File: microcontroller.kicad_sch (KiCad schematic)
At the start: 2 parts, among them U4 ESP32-S3-WROOM-1, Y1 Crystal_GND24

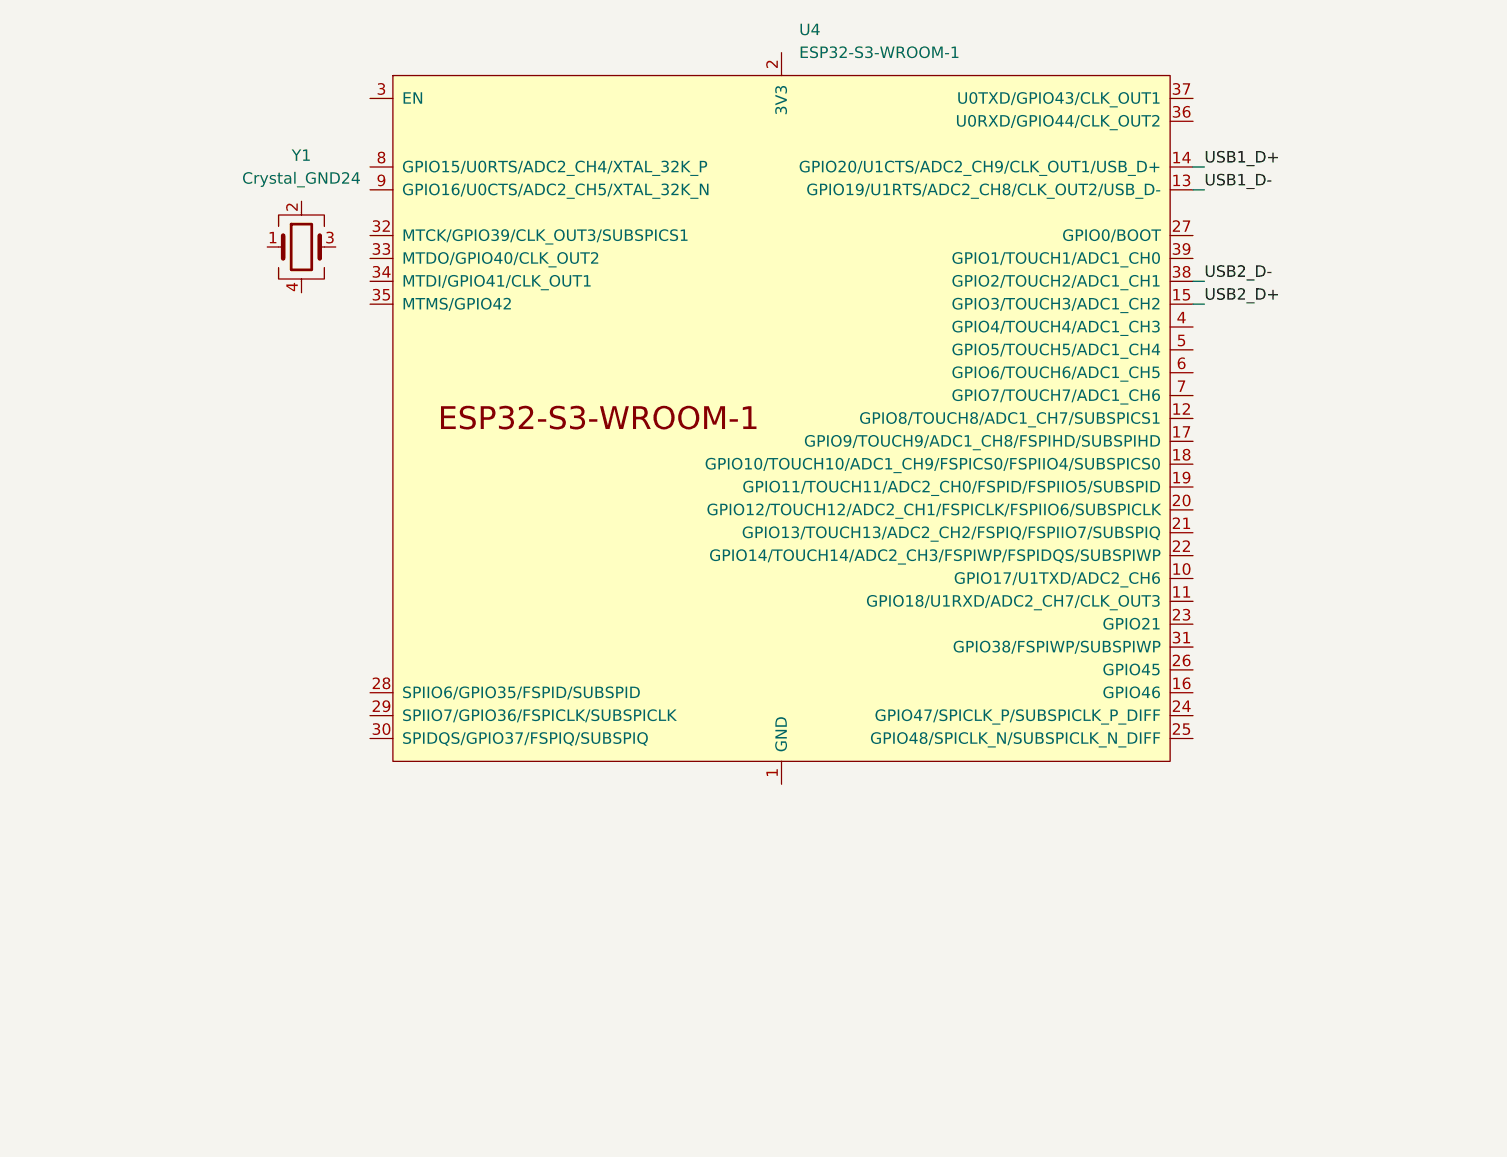
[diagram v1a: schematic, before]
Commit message: reworked component naming
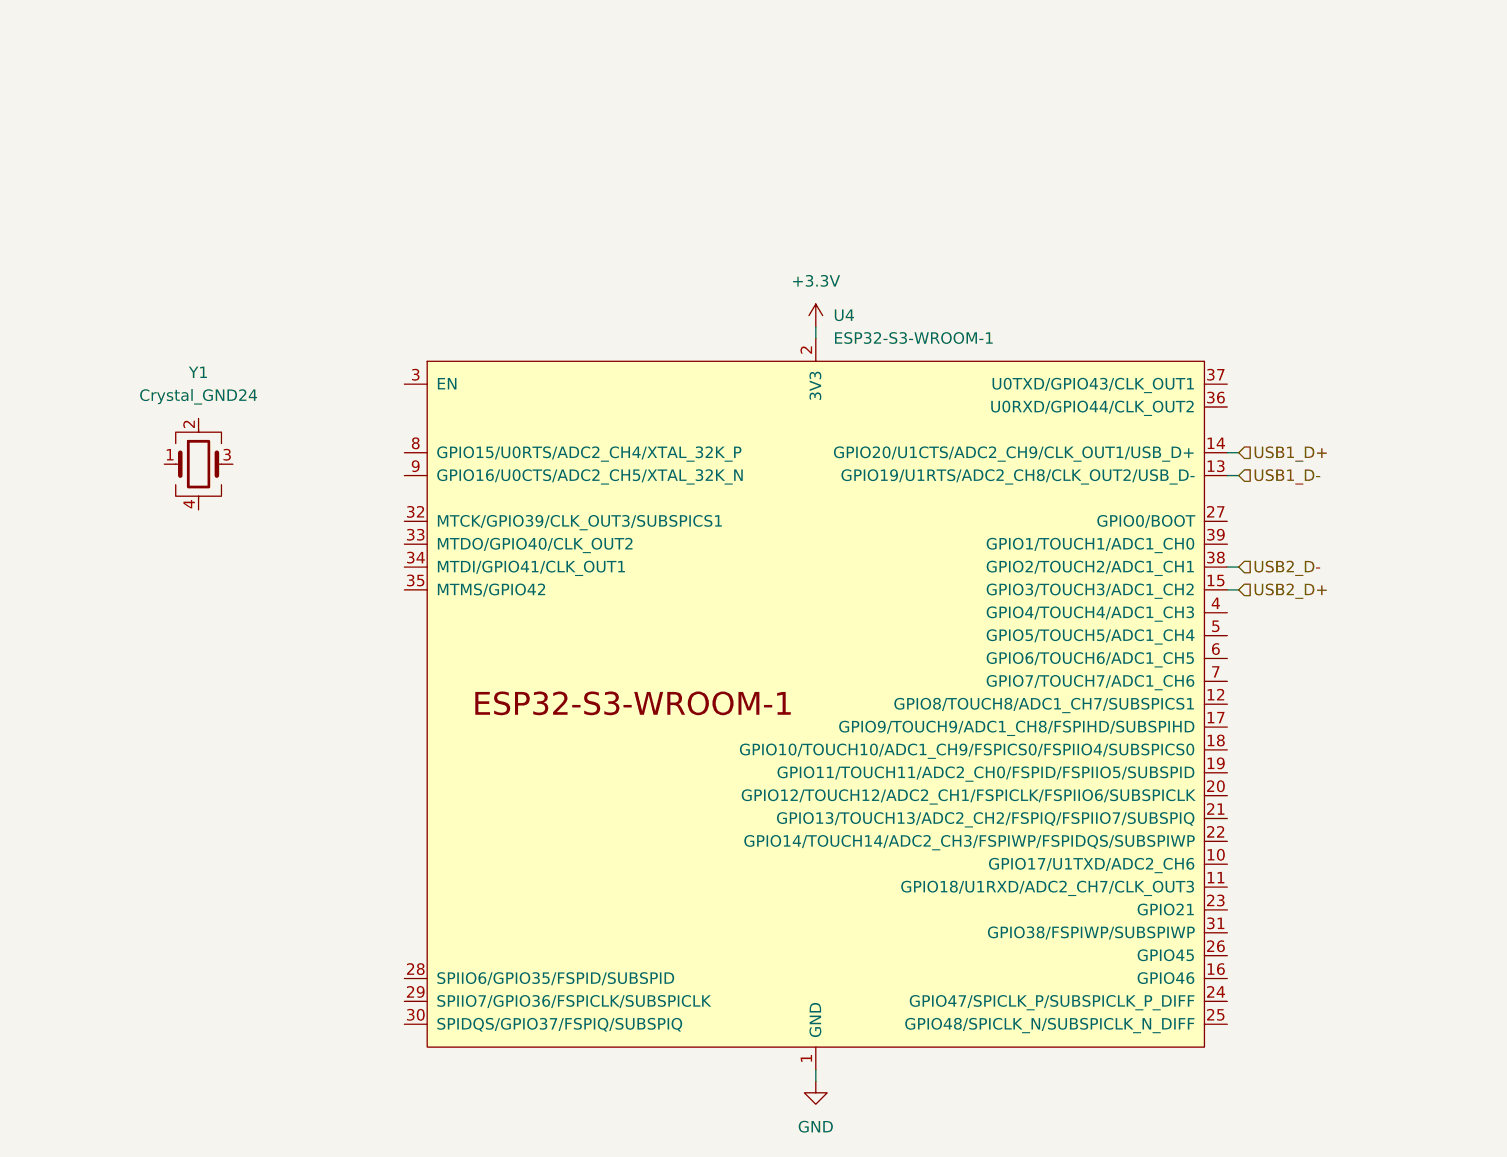
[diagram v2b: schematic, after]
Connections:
- net GND: now reaches U4.1 (GND), U4.40 (GND), U4.41 (GND)
- net +3.3V: now reaches U4.2 (3V3)
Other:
- moved on the sheet: U4, Y1
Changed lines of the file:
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@@
 (kicad_sch (version 20230121) (generator eeschema)
   (paper "A4")
-  (wire (pts (xy 156.21 50.8) (xy 154.94 50.8))
+  (wire (pts (xy 113.03 152.4) (xy 113.03 151.13))
     (stroke (width 0) (type default))
   )
-  (wire (pts (xy 156.21 63.5) (xy 154.94 63.5))
+  (wire (pts (xy 160.02 97.79) (xy 158.75 97.79))
     (stroke (width 0) (type default))
   )
-  (wire (pts (xy 154.94 53.34) (xy 156.21 53.34))
+  (wire (pts (xy 160.02 85.09) (xy 158.75 85.09))
     (stroke (width 0) (type default))
   )
-  (wire (pts (xy 156.21 66.04) (xy 154.94 66.04))
+  (wire (pts (xy 113.03 68.58) (xy 113.03 69.85))
     (stroke (width 0) (type default))
   )
-  (label "USB1_D+" (at 156.21 50.8 0) (fields_autoplaced)
-    (effects (font (size 1.27 1.27)) (justify left bottom))
+  (wire (pts (xy 160.02 82.55) (xy 158.75 82.55))
+    (stroke (width 0) (type default))
   )
-  (label "USB1_D-" (at 156.21 53.34 0) (fields_autoplaced)
-    (effects (font (size 1.27 1.27)) (justify left bottom))
+  (wire (pts (xy 160.02 95.25) (xy 158.75 95.25))
+    (stroke (width 0) (type default))
   )
-  (label "USB2_D+" (at 156.21 66.04 0) (fields_autoplaced)
-    (effects (font (size 1.27 1.27)) (justify left bottom))
+  (hierarchical_label "USB1_D-" (shape input) (at 160.02 85.09 0) (fields_autoplaced)
+    (effects (font (size 1.27 1.27)) (justify left))
   )
-  (label "USB2_D-" (at 156.21 63.5 0) (fields_autoplaced)
-    (effects (font (size 1.27 1.27)) (justify left bottom))
+  (hierarchical_label "USB1_D+" (shape input) (at 160.02 82.55 0) (fields_autoplaced)
+    (effects (font (size 1.27 1.27)) (justify left))
   )
-  (symbol (lib_id "Device:Crystal_GND24") (at 55.88 59.69 0) (unit 1)
-    (in_bom yes) (on_board yes) (dnp no)
-    (property "Reference" "Y1" (at 55.88 49.53 0)
+  (hierarchical_label "USB2_D+" (shape input) (at 160.02 97.79 0) (fields_autoplaced)
+    (effects (font (size 1.27 1.27)) (justify left))
+  )
+  (hierarchical_label "USB2_D-" (shape input) (at 160.02 95.25 0) (fields_autoplaced)
+    (effects (font (size 1.27 1.27)) (justify left))
+  )
+  (symbol (lib_id "power:+3.3V") (at 113.03 68.58 0) (unit 1)
+    (in_bom yes) (on_board yes) (dnp no) (fields_autoplaced)
+    (property "Reference" "#PWR022" (at 113.03 72.39 0)
+      (effects (font (size 1.27 1.27)) hide)
+    )
+    (property "Value" "+3.3V" (at 113.03 63.5 0)
       (effects (font (size 1.27 1.27)))
     )
-    (property "Value" "Crystal_GND24" (at 55.88 52.07 0)
+    (property "Footprint" "" (at 113.03 68.58 0)
+      (effects (font (size 1.27 1.27)) hide)
+    )
+    (property "Datasheet" "" (at 113.03 68.58 0)
+      (effects (font (size 1.27 1.27)) hide)
+    )
+    (pin "1")
+    (instances
+      (project "Lily58"
+        (path "/a0958e12-2248-4ac3-b259-3086ac296b70"
+          (reference "#PWR022") (unit 1)
+        )
+        (path "/a0958e12-2248-4ac3-b259-3086ac296b70/e89ddc09-3400-44c0-8130-3ab15c16d278"
+          (reference "#PWR05") (unit 1)
+        )
+      )
+    )
+  )
+  (symbol (lib_id "Device:Crystal_GND24") (at 44.45 83.82 0) (unit 1)
+    (in_bom yes) (on_board yes) (dnp no)
+    (property "Reference" "Y1" (at 44.45 73.66 0)
       (effects (font (size 1.27 1.27)))
     )
-    (property "Footprint" "Crystal:Crystal_SMD_3225-4Pin_3.2x2.5mm_HandSoldering" (at 55.88 59.69 0)
+    (property "Value" "Crystal_GND24" (at 44.45 76.2 0)
+      (effects (font (size 1.27 1.27)))
+    )
+    (property "Footprint" "Crystal:Crystal_SMD_3225-4Pin_3.2x2.5mm_HandSoldering" (at 44.45 83.82 0)
       (effects (font (size 1.27 1.27)) hide)
     )
-    (property "Datasheet" "~" (at 55.88 59.69 0)
+    (property "Datasheet" "~" (at 44.45 83.82 0)
       (effects (font (size 1.27 1.27)) hide)
     )
@@
     )
   )
-  (symbol (lib_id "PCM_Espressif:ESP32-S3-WROOM-1") (at 109.22 78.74 0) (unit 1)
+  (symbol (lib_id "power:GND") (at 113.03 152.4 0) (unit 1)
     (in_bom yes) (on_board yes) (dnp no) (fields_autoplaced)
-    (property "Reference" "U4" (at 111.1759 35.56 0)
+    (property "Reference" "#PWR021" (at 113.03 158.75 0)
+      (effects (font (size 1.27 1.27)) hide)
+    )
+    (property "Value" "GND" (at 113.03 157.48 0)
+      (effects (font (size 1.27 1.27)))
+    )
+    (property "Footprint" "" (at 113.03 152.4 0)
+      (effects (font (size 1.27 1.27)) hide)
+    )
+    (property "Datasheet" "" (at 113.03 152.4 0)
+      (effects (font (size 1.27 1.27)) hide)
+    )
+    (pin "1")
+    (instances
+      (project "Lily58"
+        (path "/a0958e12-2248-4ac3-b259-3086ac296b70"
+          (reference "#PWR021") (unit 1)
+        )
+        (path "/a0958e12-2248-4ac3-b259-3086ac296b70/e89ddc09-3400-44c0-8130-3ab15c16d278"
+          (reference "#PWR015") (unit 1)
+        )
+      )
+    )
+  )
+  (symbol (lib_id "PCM_Espressif:ESP32-S3-WROOM-1") (at 113.03 110.49 0) (unit 1)
+    (in_bom yes) (on_board yes) (dnp no) (fields_autoplaced)
+    (property "Reference" "U4" (at 114.9859 67.31 0)
       (effects (font (size 1.27 1.27)) (justify left))
     )
-    (property "Value" "ESP32-S3-WROOM-1" (at 111.1759 38.1 0)
+    (property "Value" "ESP32-S3-WROOM-1" (at 114.9859 69.85 0)
       (effects (font (size 1.27 1.27)) (justify left))
     )
-    (property "Footprint" "PCM_Espressif:ESP32-S3-WROOM-1" (at 111.76 127 0)
+    (property "Footprint" "PCM_Espressif:ESP32-S3-WROOM-1" (at 115.57 158.75 0)
       (effects (font (size 1.27 1.27)) hide)
     )
-    (property "Datasheet" "https://www.espressif.com/sites/default/files/documentation/esp32-s3-wroom-1_wroom-1u_datasheet_en.pdf" (at 111.76 129.54 0)
+    (property "Datasheet" "https://www.espressif.com/sites/default/files/documentation/esp32-s3-wroom-1_wroom-1u_datasheet_en.pdf" (at 115.57 161.29 0)
       (effects (font (size 1.27 1.27)) hide)
     )

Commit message: added ESP32 circuitry
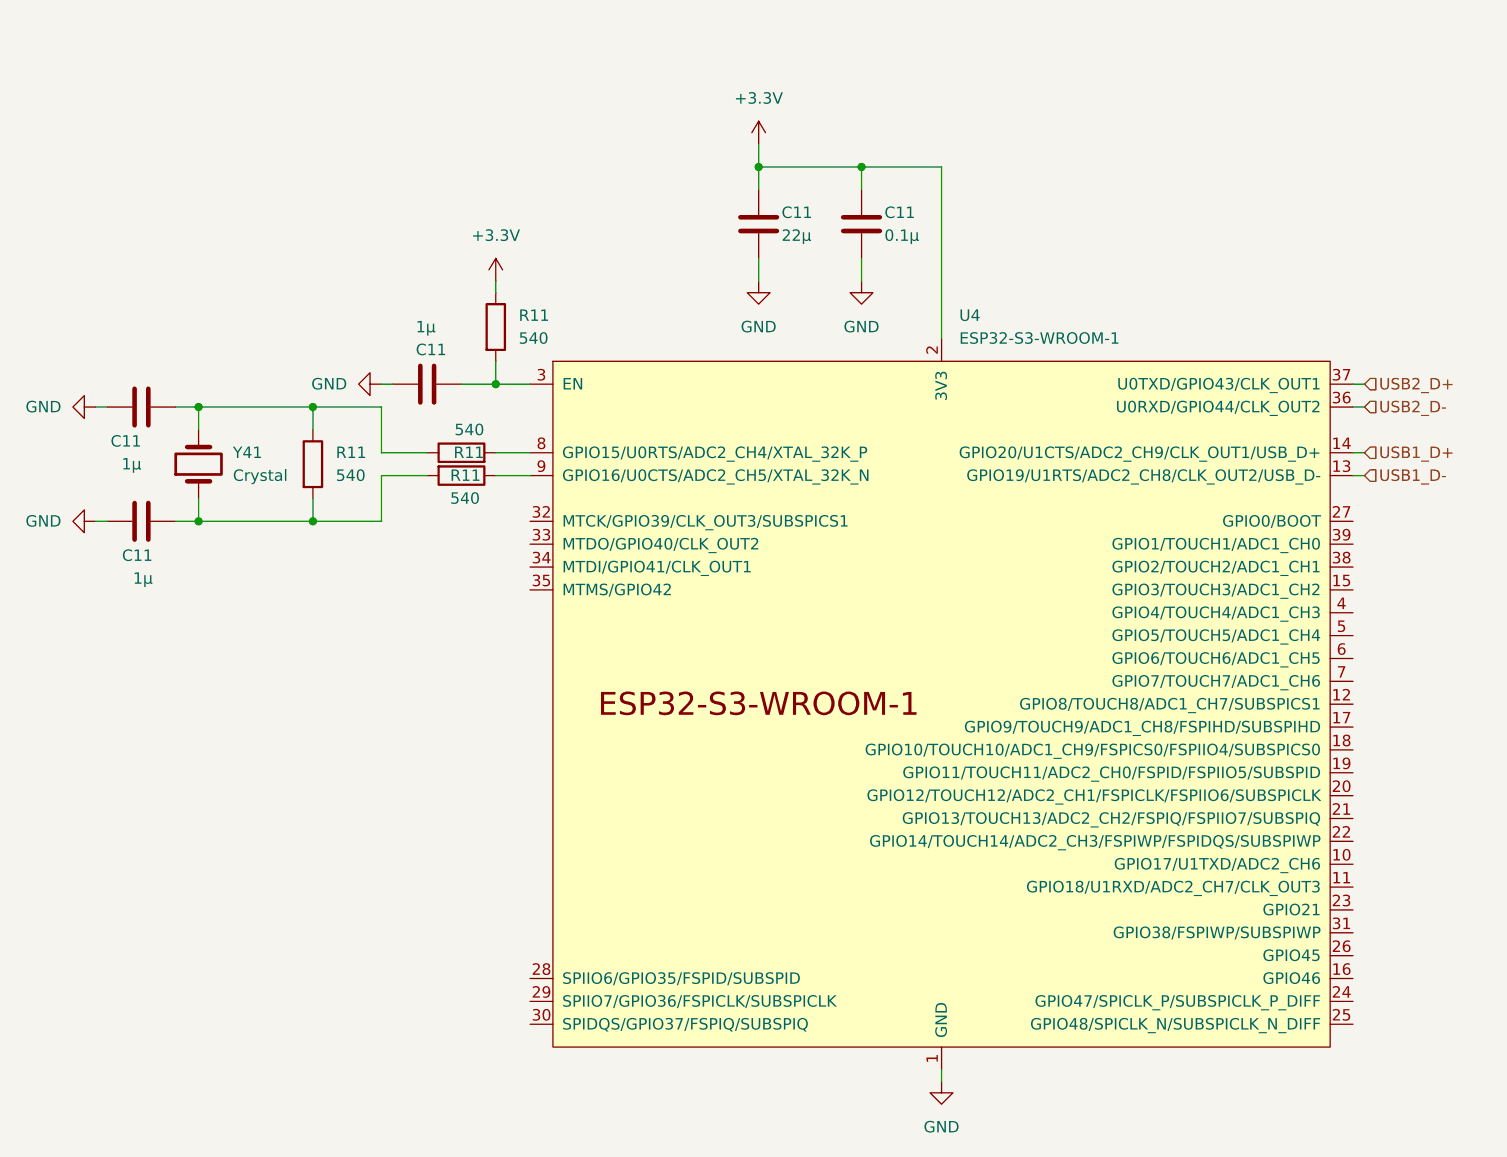
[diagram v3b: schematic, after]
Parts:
- removed Y1: Crystal_GND24, Crystal:Crystal_SMD_3225-4Pin_3.2x2.5mm_HandSoldering, symbol Device:Crystal_GND24
- added C11: 22µ, symbol Device:C
- added C11 (x3): 1µ, symbol Device:C
- added C11: 0.1µ, symbol Device:C
- added R11 (x4): 540, symbol Device:R
- added Y41: Crystal, symbol Device:Crystal
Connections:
- net +3.3V: now also C11.1, C11.1, R11.1
- net GND: now also C11.1, C11.1, C11.2, C11.2, C11.2
- net USB2_D+: now also U4.37 (U0TXD/GPIO43/CLK_OUT1); no longer U4.15 (GPIO3/TOUCH3/ADC1_CH2)
- net USB2_D-: now also U4.36 (U0RXD/GPIO44/CLK_OUT2); no longer U4.38 (GPIO2/TOUCH2/ADC1_CH1)
- net at U4.3 (EN): now also C11.1, R11.2
- net at U4.8 (GPIO15/U0RTS/ADC2_CH4/XTAL_32K_P): now also R11.2
- net at U4.9 (GPIO16/U0CTS/ADC2_CH5/XTAL_32K_N): now also R11.1
- new net: C11.2, R11.1, R11.1, Y41.2
- new net: C11.2, R11.2, R11.2, Y41.1
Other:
- moved on the sheet: U4
